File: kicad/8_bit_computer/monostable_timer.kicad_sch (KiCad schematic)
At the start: 9 parts, among them U1 NE555P

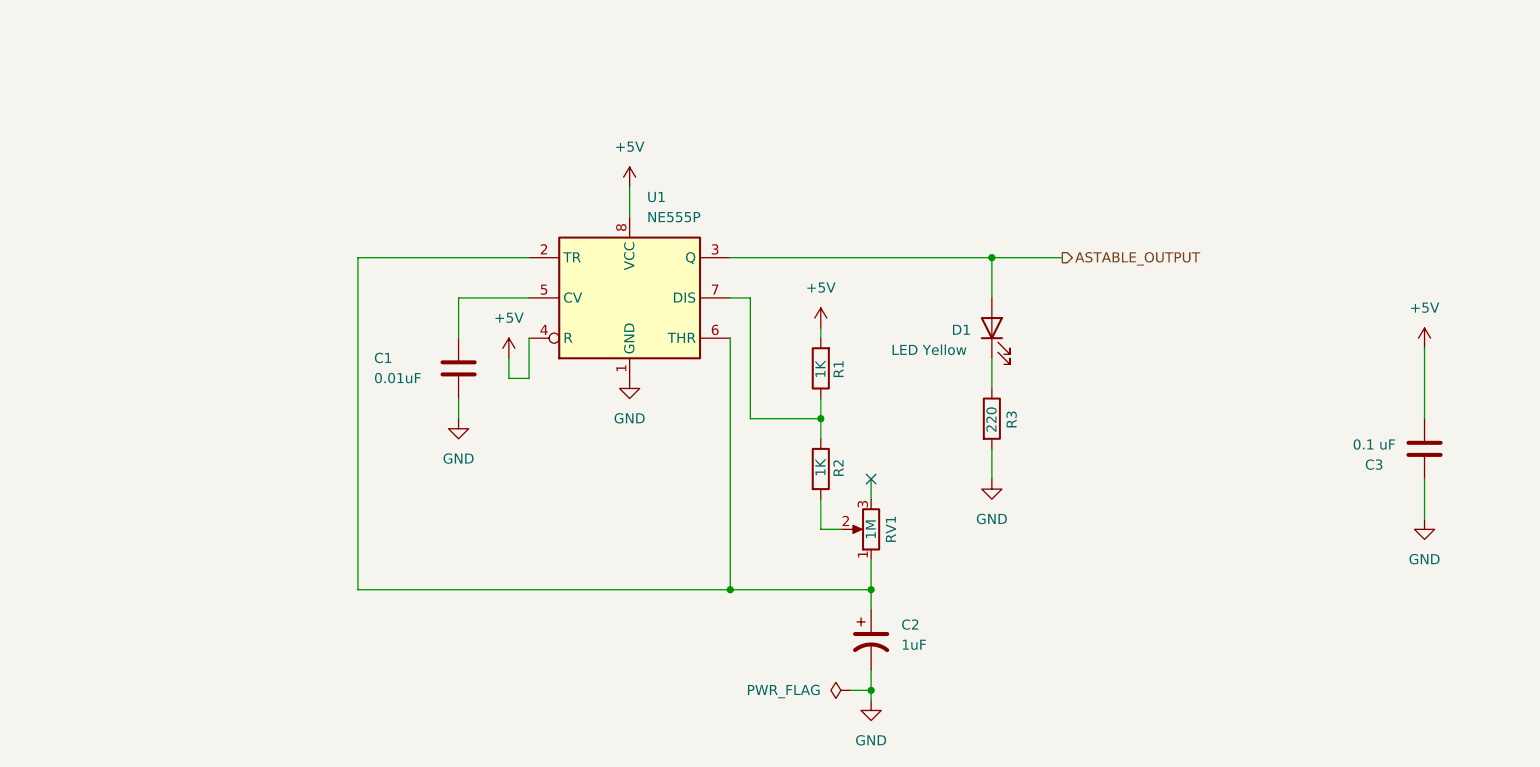
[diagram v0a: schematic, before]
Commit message: Bistable and Monstable Clocks
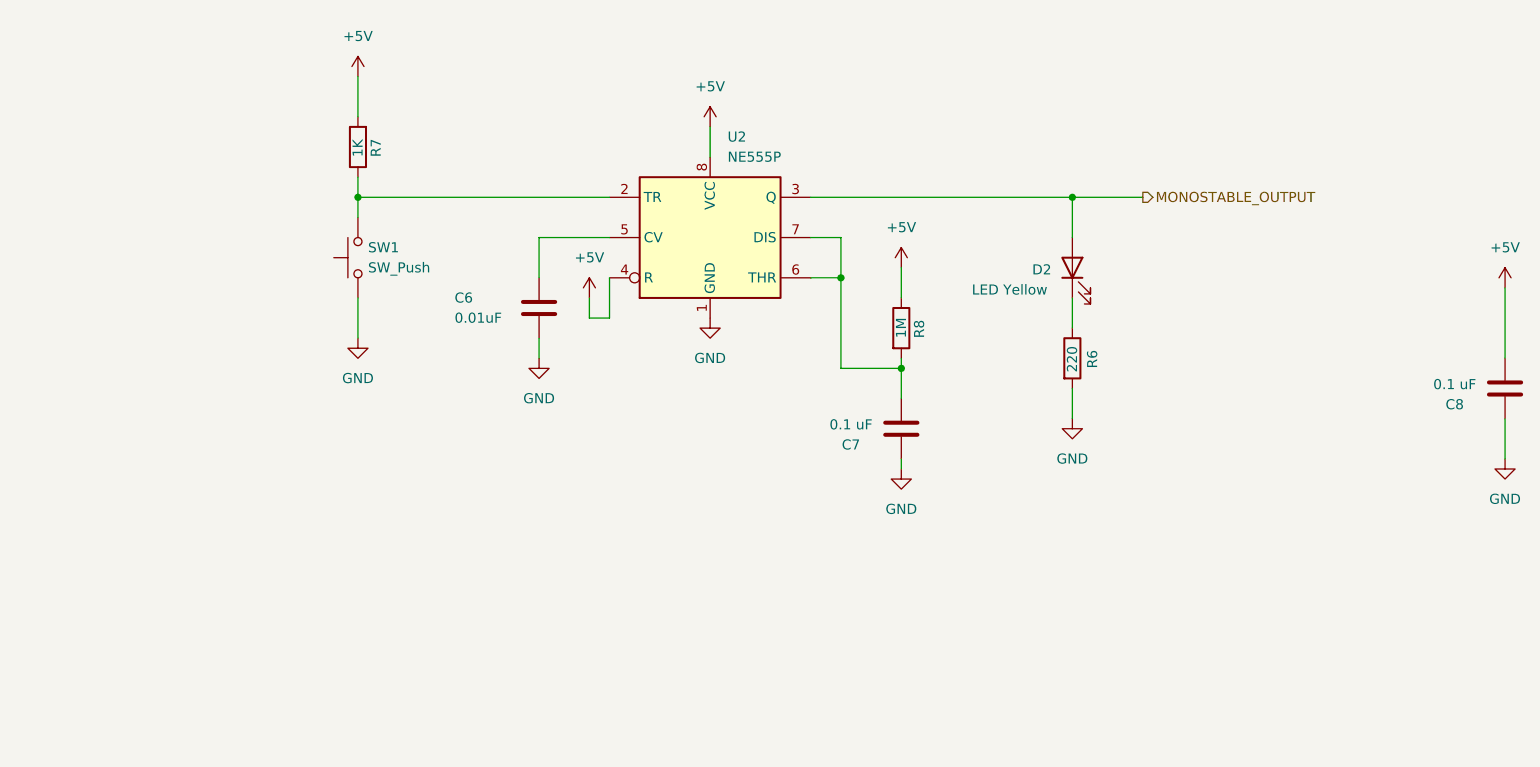
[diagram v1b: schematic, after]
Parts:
- removed C1: 0.01uF, Capacitor_THT:C_Disc_D5.0mm_W2.5mm_P2.50mm, symbol Device:C
- removed C2: 1uF, Capacitor_THT:CP_Radial_D5.0mm_P2.00mm, symbol Device:C_Polarized_US
- removed C3: 0.1 uF, Capacitor_THT:C_Disc_D5.0mm_W2.5mm_P2.50mm, symbol Device:C
- removed D1: LED Yellow, LED_THT:LED_D5.0mm, symbol Device:LED
- removed R1, R2: 1K, Resistor_THT:R_Axial_DIN0207_L6.3mm_D2.5mm_P7.62mm_Horizontal, symbol Device:R
- removed R3: 220, Resistor_THT:R_Axial_DIN0207_L6.3mm_D2.5mm_P7.62mm_Horizontal, symbol Device:R
- removed RV1: 1M, 8-bit-computer-custom-footprints:Potentiometer_CT-6EP105, symbol Device:R_Potentiometer
- removed U1: NE555P, Package_DIP:DIP-8_W7.62mm, symbol Timer:NE555P
- added C6: 0.01uF, Capacitor_THT:C_Disc_D5.0mm_W2.5mm_P2.50mm, symbol Device:C
- added C7, C8: 0.1 uF, Capacitor_THT:C_Disc_D5.0mm_W2.5mm_P2.50mm, symbol Device:C
- added D2: LED Yellow, LED_THT:LED_D5.0mm, symbol Device:LED
- added R6: 220, Resistor_THT:R_Axial_DIN0207_L6.3mm_D2.5mm_P7.62mm_Horizontal, symbol Device:R
- added R7: 1K, Resistor_THT:R_Axial_DIN0207_L6.3mm_D2.5mm_P7.62mm_Horizontal, symbol Device:R
- added R8: 1M, Resistor_THT:R_Axial_DIN0207_L6.3mm_D2.5mm_P7.62mm_Horizontal, symbol Device:R
- added SW1: SW_Push, Button_Switch_THT:SW_PUSH_6mm, symbol Switch:SW_Push
- added U2: NE555P, Package_DIP:DIP-8_W7.62mm, symbol Timer:NE555P
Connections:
- net +5V: now also C8.2, R7.2, R8.1, U2.4 (R), U2.8 (VCC)
- net GND: now also C6.2, C7.1, C8.1, R6.2, SW1.1, U2.1 (GND)
- new net: D2.1 (K), R6.1
- new net: R7.1, SW1.2, U2.2 (TR)
- new net: C6.1, U2.5 (CV)
- new net: C7.2, R8.2, U2.6 (THR), U2.7 (DIS)
- new net MONOSTABLE_OUTPUT: D2.2 (A), U2.3 (Q)
- no-connect marks 1 -> 0
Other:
- title: Astable Timer -> (none)

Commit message: Mostly implemented register, still ERC errors
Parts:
- removed C8: 0.1 uF, Capacitor_THT:C_Disc_D5.0mm_W2.5mm_P2.50mm, symbol Device:C
- added C20, C3: 0.1 uF, Capacitor_THT:C_Disc_D5.0mm_W2.5mm_P2.50mm, symbol Device:C
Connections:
- net +5V: now also C20.1, C3.2
- net GND: now also C20.2, C3.1
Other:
- moved on the sheet: C6

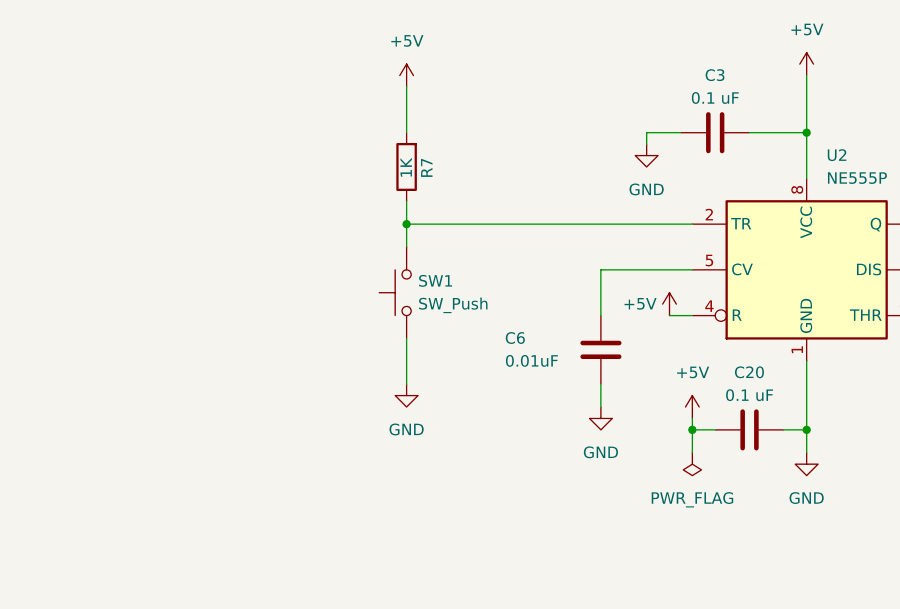
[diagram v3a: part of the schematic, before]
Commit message: Add pull up/down resistors to all vcc/gnd shorts
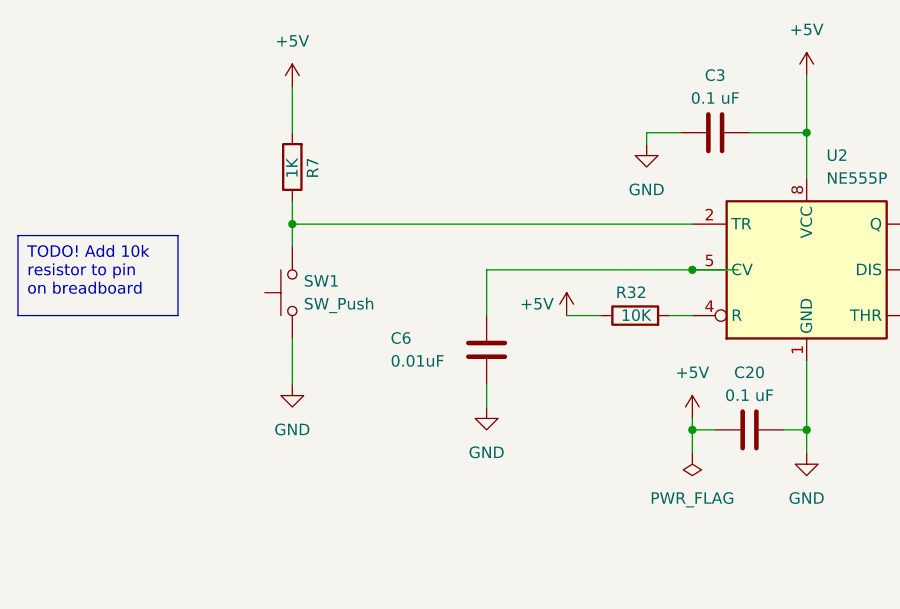
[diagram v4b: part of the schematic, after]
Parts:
- added R32: 10K, Resistor_THT:R_Axial_DIN0207_L6.3mm_D2.5mm_P7.62mm_Horizontal, symbol Device:R
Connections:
- net +5V: now also R32.1; no longer U2.4 (R)
- new net: R32.2, U2.4 (R)
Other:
- moved on the sheet: C6, R7, SW1
